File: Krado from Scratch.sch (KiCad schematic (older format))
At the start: 12 parts

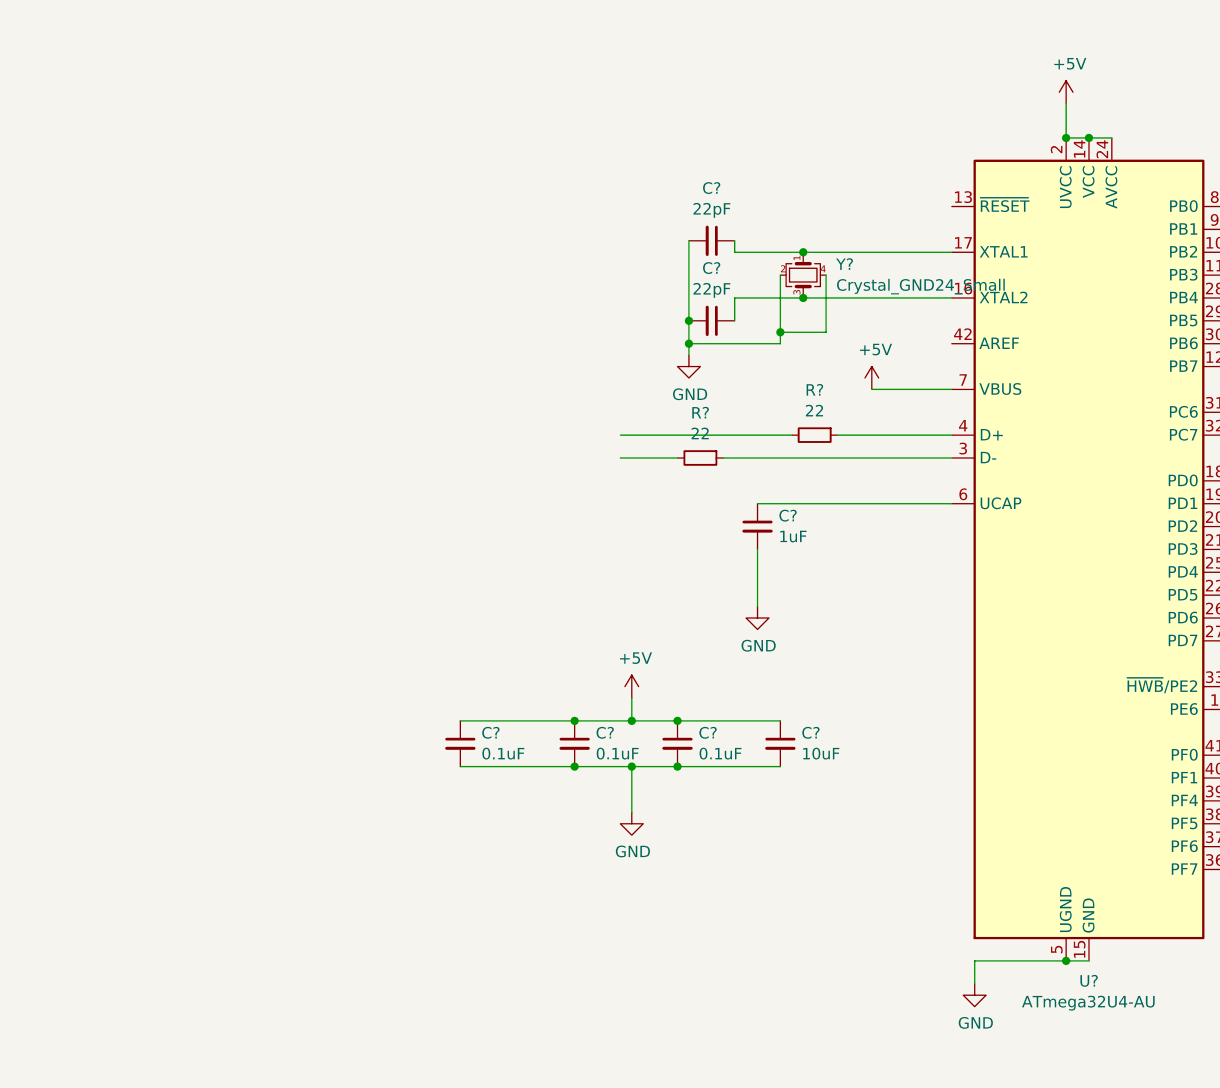
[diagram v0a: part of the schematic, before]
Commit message: USB-C Added
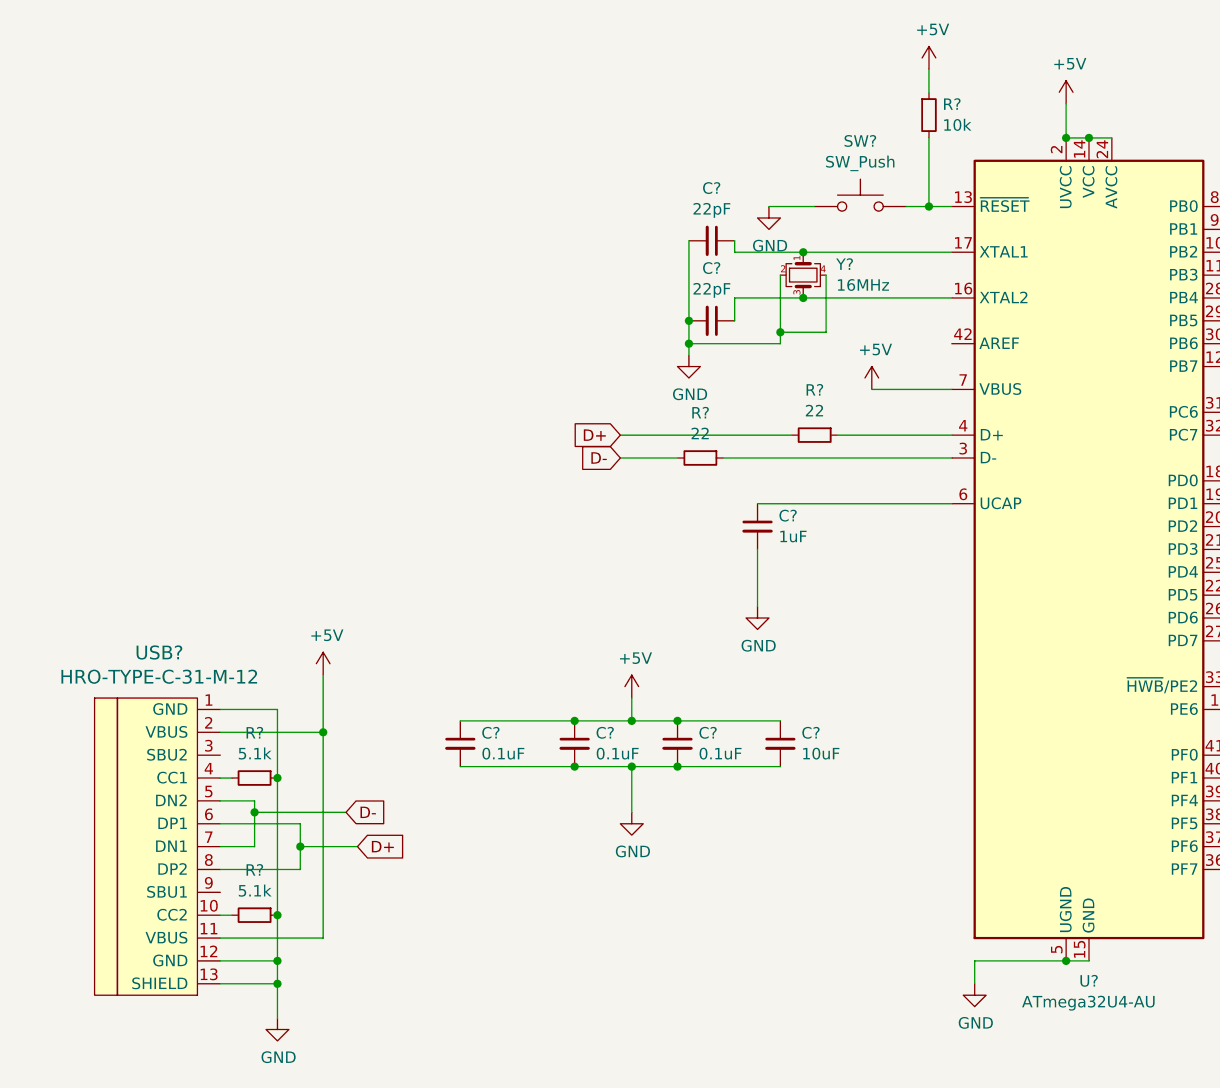
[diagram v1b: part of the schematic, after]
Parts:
- added R?: 10k, symbol Device:R_Small
- added R? (x2): 5.1k, symbol Device:R_Small
- added SW?: SW_Push, symbol Switch:SW_Push
- added USB?: HRO-TYPE-C-31-M-12, symbol Type-C:HRO-TYPE-C-31-M-12
- Y?: value Crystal_GND24_Small -> 16MHz
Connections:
- net labels added: D+, D-
- wire segments 39 -> 68
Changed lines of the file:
@@
 P 9150 3200
 F 0 "Y?" V 9104 3344 50  0000 L CNN
-F 1 "Crystal_GND24_Small" V 9195 3344 50  0000 L CNN
+F 1 "16MHz" V 9195 3344 50  0000 L CNN
 F 2 "" H 9150 3200 50  0001 C CNN
 F 3 "~" H 9150 3200 50  0001 C CNN
@@
 Wire Wire Line
 	9050 3450 9050 3500
+$Comp
+L Switch:SW_Push SW?
+U 1 1 60753B4A
+P 9400 2900
+F 0 "SW?" H 9400 3185 50  0000 C CNN
+F 1 "SW_Push" H 9400 3094 50  0000 C CNN
+F 2 "" H 9400 3100 50  0001 C CNN
+F 3 "~" H 9400 3100 50  0001 C CNN
+	1    9400 2900
+	1    0    0    -1
+$EndComp
+$Comp
+L power:GND #PWR?
+U 1 1 60755F3E
+P 9000 2900
+F 0 "#PWR?" H 9000 2650 50  0001 C CNN
+F 1 "GND" H 9005 2727 50  0000 C CNN
+F 2 "" H 9000 2900 50  0001 C CNN
+F 3 "" H 9000 2900 50  0001 C CNN
+	1    9000 2900
+	1    0    0    -1
+$EndComp
+Wire Wire Line
+	9000 2900 9200 2900
+Wire Wire Line
+	9600 2900 9700 2900
+Wire Wire Line
+	9700 2900 9700 2600
+Connection ~ 9700 2900
+Wire Wire Line
+	9700 2900 9800 2900
+$Comp
+L Device:R_Small R?
+U 1 1 60759043
+P 9700 2500
+F 0 "R?" H 9759 2546 50  0000 L CNN
+F 1 "10k" H 9759 2455 50  0000 L CNN
+F 2 "" H 9700 2500 50  0001 C CNN
+F 3 "~" H 9700 2500 50  0001 C CNN
+	1    9700 2500
+	1    0    0    -1
+$EndComp
+$Comp
+L power:+5V #PWR?
+U 1 1 6075A732
+P 9700 2300
+F 0 "#PWR?" H 9700 2150 50  0001 C CNN
+F 1 "+5V" H 9715 2473 50  0000 C CNN
+F 2 "" H 9700 2300 50  0001 C CNN
+F 3 "" H 9700 2300 50  0001 C CNN
+	1    9700 2300
+	1    0    0    -1
+$EndComp
+Wire Wire Line
+	9700 2400 9700 2300
+Text GLabel 8350 3900 0    50   Input ~ 0
+D+
+Text GLabel 8350 4000 0    50   Input ~ 0
+D-
+$Comp
+L Type-C:HRO-TYPE-C-31-M-12 USB?
+U 1 1 6075E2AA
+P 6500 5650
+F 0 "USB?" H 6333 6447 60  0000 C CNN
+F 1 "HRO-TYPE-C-31-M-12" H 6333 6341 60  0000 C CNN
+F 2 "" H 6500 5650 60  0001 C CNN
+F 3 "" H 6500 5650 60  0001 C CNN
+	1    6500 5650
+	1    0    0    -1
+$EndComp
+$Comp
+L power:+5V #PWR?
+U 1 1 60764690
+P 7050 4950
+F 0 "#PWR?" H 7050 4800 50  0001 C CNN
+F 1 "+5V" H 7065 5123 50  0000 C CNN
+F 2 "" H 7050 4950 50  0001 C CNN
+F 3 "" H 7050 4950 50  0001 C CNN
+	1    7050 4950
+	1    0    0    -1
+$EndComp
+Wire Wire Line
+	6600 5200 7050 5200
+Wire Wire Line
+	7050 5200 7050 4950
+Wire Wire Line
+	6600 6100 7050 6100
+Wire Wire Line
+	7050 6100 7050 5200
+Connection ~ 7050 5200
+$Comp
+L power:GND #PWR?
+U 1 1 60767AC1
+P 6850 6450
+F 0 "#PWR?" H 6850 6200 50  0001 C CNN
+F 1 "GND" H 6855 6277 50  0000 C CNN
+F 2 "" H 6850 6450 50  0001 C CNN
+F 3 "" H 6850 6450 50  0001 C CNN
+	1    6850 6450
+	1    0    0    -1
+$EndComp
+Wire Wire Line
+	6600 5100 6850 5100
+Wire Wire Line
+	6600 6200 6850 6200
+Connection ~ 6850 6200
+Wire Wire Line
+	6850 6200 6850 6300
+Wire Wire Line
+	6600 6300 6850 6300
+Connection ~ 6850 6300
+Wire Wire Line
+	6850 6300 6850 6450
+Wire Wire Line
+	6600 5500 6750 5500
+Wire Wire Line
+	6750 5500 6750 5550
+Wire Wire Line
+	6750 5700 6600 5700
+Wire Wire Line
+	6600 5600 6950 5600
+Wire Wire Line
+	6950 5600 6950 5700
+Wire Wire Line
+	6950 5800 6600 5800
+Wire Wire Line
+	6750 5550 7150 5550
+Connection ~ 6750 5550
+Wire Wire Line
+	6750 5550 6750 5700
+Wire Wire Line
+	6950 5700 7200 5700
+Connection ~ 6950 5700
+Wire Wire Line
+	6950 5700 6950 5800
+Text GLabel 7200 5700 2    50   Input ~ 0
+D+
+Text GLabel 7150 5550 2    50   Input ~ 0
+D-
+Wire Wire Line
+	6850 5100 6850 5400
+$Comp
+L Device:R_Small R?
+U 1 1 60777EB7
+P 6750 5400
+F 0 "R?" V 6554 5400 50  0000 C CNN
+F 1 "5.1k" V 6645 5400 50  0000 C CNN
+F 2 "" H 6750 5400 50  0001 C CNN
+F 3 "~" H 6750 5400 50  0001 C CNN
+	1    6750 5400
+	0    1    1    0
+$EndComp
+Connection ~ 6850 5400
+Wire Wire Line
+	6850 5400 6850 6000
+$Comp
+L Device:R_Small R?
+U 1 1 607796CE
+P 6750 6000
+F 0 "R?" V 6554 6000 50  0000 C CNN
+F 1 "5.1k" V 6645 6000 50  0000 C CNN
+F 2 "" H 6750 6000 50  0001 C CNN
+F 3 "~" H 6750 6000 50  0001 C CNN
+	1    6750 6000
+	0    1    1    0
+$EndComp
+Connection ~ 6850 6000
+Wire Wire Line
+	6850 6000 6850 6200
+Wire Wire Line
+	6650 6000 6600 6000
+Wire Wire Line
+	6650 5400 6600 5400
 $EndSCHEMATC

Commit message: MATRI
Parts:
- added D? (x64): SOD-123, symbol Device:D_Small
- added MX? (x69): MX-NoLED, symbol MX_Alps_Hybrid:MX-NoLED
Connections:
- new net: D?.2 (A), MX?.2 (ROW) (x59)
- new net: D?.2 (A), MX?.2 (ROW), MX?.2 (ROW) (x5)
- new net COL0: MX?.1 (COL), MX?.1 (COL)
- new net COL1: MX?.1 (COL), MX?.1 (COL), MX?.1 (COL), MX?.1 (COL), MX?.1 (COL)
- new net COL10: MX?.1 (COL), MX?.1 (COL), MX?.1 (COL), MX?.1 (COL), MX?.1 (COL)
- new net COL11: MX?.1 (COL), MX?.1 (COL), MX?.1 (COL), MX?.1 (COL), MX?.1 (COL)
- new net COL12: MX?.1 (COL), MX?.1 (COL), MX?.1 (COL), MX?.1 (COL), MX?.1 (COL)
- new net COL13: MX?.1 (COL), MX?.1 (COL), MX?.1 (COL), MX?.1 (COL), MX?.1 (COL)
- new net COL14: MX?.1 (COL), MX?.1 (COL), MX?.1 (COL), MX?.1 (COL)
- new net COL15: MX?.1 (COL), MX?.1 (COL), MX?.1 (COL)
- new net COL2: MX?.1 (COL), MX?.1 (COL), MX?.1 (COL), MX?.1 (COL), MX?.1 (COL)
- new net COL3: MX?.1 (COL), MX?.1 (COL), MX?.1 (COL), MX?.1 (COL)
- new net COL4: MX?.1 (COL), MX?.1 (COL), MX?.1 (COL), MX?.1 (COL)
- new net COL5: MX?.1 (COL), MX?.1 (COL), MX?.1 (COL), MX?.1 (COL)
- new net COL6: MX?.1 (COL), MX?.1 (COL), MX?.1 (COL), MX?.1 (COL), MX?.1 (COL)
- new net COL7: MX?.1 (COL), MX?.1 (COL), MX?.1 (COL), MX?.1 (COL)
- new net COL9: MX?.1 (COL), MX?.1 (COL), MX?.1 (COL), MX?.1 (COL)
- new net ROW0: D?.1 (K), D?.1 (K), D?.1 (K), D?.1 (K), D?.1 (K), D?.1 (K), D?.1 (K), D?.1 (K), D?.1 (K), D?.1 (K), D?.1 (K), D?.1 (K), D?.1 (K), D?.1 (K), D?.1 (K)
- new net ROW1: D?.1 (K), D?.1 (K), D?.1 (K), D?.1 (K), D?.1 (K), D?.1 (K), D?.1 (K), D?.1 (K), D?.1 (K), D?.1 (K), D?.1 (K), D?.1 (K), D?.1 (K)
- new net ROW2: D?.1 (K), D?.1 (K), D?.1 (K), D?.1 (K), D?.1 (K), D?.1 (K), D?.1 (K), D?.1 (K), D?.1 (K), D?.1 (K), D?.1 (K), D?.1 (K)
- new net ROW3: D?.1 (K), D?.1 (K), D?.1 (K), D?.1 (K), D?.1 (K), D?.1 (K), D?.1 (K), D?.1 (K), D?.1 (K), D?.1 (K), D?.1 (K), D?.1 (K), D?.1 (K), D?.1 (K)
- new net ROW4: D?.1 (K), D?.1 (K), D?.1 (K), D?.1 (K), D?.1 (K), D?.1 (K), D?.1 (K), D?.1 (K), D?.1 (K), D?.1 (K)
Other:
- moved on the sheet: C?, R?, SW?, U?, USB?, Y?

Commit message: Matrix Fixed
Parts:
- removed D?: SOD-123, symbol Device:D_Small
- removed MX?: MX-NoLED, symbol MX_Alps_Hybrid:MX-NoLED
- added D? (x4): SOD-123, symbol Device:D_Small
- added KY_8, KY_I, MX? (x2): MX-NoLED, symbol MX_Alps_Hybrid:MX-NoLED
- gave numbers to parts that had none: 28
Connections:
- net COL1: now also MX?.1 (COL)
- net COL10: now also MX?.1 (COL)
- net COL11: now also MX?.1 (COL)
- net COL12: now also MX?.1 (COL)
- net COL14: now also MX?.1 (COL)
- net COL9: now also KY_8.1 (COL); no longer KY_7.1 (COL), KY_U.1 (COL), MX?.1 (COL), MX?.1 (COL)
- net ROW0: now also D?.1 (K)
- net ROW1: now also D?.1 (K)
- net ROW2: now also D?.1 (K)
- net ROW3: now also D?.1 (K)
- new net: D?.2 (A), KY_8.2 (ROW)
- new net: D?.2 (A), KY_I.2 (ROW)
- new net: D?.2 (A), MX?.2 (ROW) (x2)
- new net COL8: KY_7.1 (COL), KY_U.1 (COL), MX?.1 (COL), MX?.1 (COL)
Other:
- moved on the sheet: BACKSPLIT1, BACKSPLIT2, D?, KY_0, KY_9, KY_BAR, KY_EQUALS, KY_LBRACK, KY_MINUS, KY_O, KY_P, KY_RBRACK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

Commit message: Matrix Named
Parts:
- gave numbers to parts that had none: 40
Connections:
- net COL9: now also KY_COMMA.1 (COL), KY_I.1 (COL), KY_K.1 (COL)

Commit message: PCB Generated
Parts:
- added F1: 500mA, Fuse:Fuse_1206_3216Metric, symbol Device:Polyfuse_Small
- 1.25U_PN2, 1.25U_R_ALT1: renamed from MX?; footprint (none) -> MX_Only:MXOnly-1.25U-Hotswap
- 1U_PN1: renamed from PN; footprint (none) -> MX_Only:MXOnly-1U-Hotswap
- 1U_R_ALT1: renamed from R_ALT; footprint (none) -> MX_Only:MXOnly-1U-Hotswap
- 2.75U_SHIFT1: renamed from 2.75U_SHIFT; footprint (none) -> MX_Only:MXOnly-2.75U-Hotswap
- 2U_BACKSPACE1: renamed from 2U_BACKSPACE; footprint (none) -> MX_Only:MXOnly-2U-Hotswap
- BACKSPLIT1, BACKSPLIT2, KY_0, KY_1, KY_2, KY_3, KY_4, KY_5, KY_6, KY_7, KY_8, KY_9: footprint (none) -> MX_Only:MXOnly-1U-Hotswap
- C1, C2, C3, C4, C5, C6, C7: renamed from C?; footprint (none) -> Diode_SMD:D_SOD-123
- D1, D10, D11, D12, D13, D14, D15, D16, D17, D18, D19, D2, D20, D21, D22, D23, D24, D25, D26, D27, D28, D29, D3, D30, D31, D32, D33, D34, D35, D36, D37, D38, D39, D4, D40, D41, D42, D43, D44, D45, D46, D47, D48, D49, D5, D50, D51, D52, D53, D54, D55, D56, D57, D58, D59, D6, D60, D61, D62, D63, D64, D65, D66, D67, D7, D8, D9: renamed from D?; footprint (none) -> Diode_SMD:D_SOD-123
- DOWNARROW1: renamed from DOWNARROW; footprint (none) -> MX_Only:MXOnly-1U-Hotswap
- FN1: renamed from FN; footprint (none) -> MX_Only:MXOnly-1U-Hotswap
- KY_A1: renamed from KY_A; footprint (none) -> MX_Only:MXOnly-1U-Hotswap
- KY_B1: renamed from KY_B; footprint (none) -> MX_Only:MXOnly-1U-Hotswap
- KY_BAR1: renamed from KY_BAR; footprint (none) -> MX_Only:MXOnly-1U-Hotswap
- KY_C1: renamed from KY_C; footprint (none) -> MX_Only:MXOnly-1U-Hotswap
- KY_COLON1: renamed from KY_COLON; footprint (none) -> MX_Only:MXOnly-1U-Hotswap
- KY_COMMA1: renamed from KY_COMMA; footprint (none) -> MX_Only:MXOnly-1U-Hotswap
- KY_D1: renamed from KY_D; footprint (none) -> MX_Only:MXOnly-1U-Hotswap
- KY_E1: renamed from KY_E; footprint (none) -> MX_Only:MXOnly-1U-Hotswap
- KY_EQUALS1: renamed from KY_EQUALS; footprint (none) -> MX_Only:MXOnly-1U-Hotswap
- KY_ESC1: renamed from KY_ESC; footprint (none) -> MX_Only:MXOnly-1U-Hotswap
- KY_F1: renamed from KY_F; footprint (none) -> MX_Only:MXOnly-1U-Hotswap
- KY_G1: renamed from KY_G; footprint (none) -> MX_Only:MXOnly-1U-Hotswap
- KY_GRAVE1: renamed from KY_GRAVE; footprint (none) -> MX_Only:MXOnly-1U-Hotswap
- KY_H1: renamed from KY_H; footprint (none) -> MX_Only:MXOnly-1U-Hotswap
- KY_I1: renamed from KY_I; footprint (none) -> MX_Only:MXOnly-1U-Hotswap
- KY_J1: renamed from KY_J; footprint (none) -> MX_Only:MXOnly-1U-Hotswap
- KY_K1: renamed from KY_K; footprint (none) -> MX_Only:MXOnly-1U-Hotswap
- KY_L1: renamed from KY_L; footprint (none) -> MX_Only:MXOnly-1U-Hotswap
- KY_LBRACK1: renamed from KY_LBRACK; footprint (none) -> MX_Only:MXOnly-1U-Hotswap
- KY_M1: renamed from KY_M; footprint (none) -> MX_Only:MXOnly-1U-Hotswap
- KY_MINUS1: renamed from KY_MINUS; footprint (none) -> MX_Only:MXOnly-1U-Hotswap
- KY_N1: renamed from KY_N; footprint (none) -> MX_Only:MXOnly-1U-Hotswap
- KY_O1: renamed from KY_O; footprint (none) -> MX_Only:MXOnly-1U-Hotswap
- KY_P1: renamed from KY_P; footprint (none) -> MX_Only:MXOnly-1U-Hotswap
- KY_PERIOD1: renamed from KY_PERIOD; footprint (none) -> MX_Only:MXOnly-1U-Hotswap
- KY_Q1: renamed from KY_Q; footprint (none) -> MX_Only:MXOnly-1U-Hotswap
- KY_QUESTION1: renamed from KY_QUESTION; footprint (none) -> MX_Only:MXOnly-1U-Hotswap
- KY_QUOTE1: renamed from KY_QUOTE; footprint (none) -> MX_Only:MXOnly-1U-Hotswap
- KY_R1: renamed from KY_R; footprint (none) -> MX_Only:MXOnly-1U-Hotswap
- KY_RBRACK1: renamed from KY_RBRACK; footprint (none) -> MX_Only:MXOnly-1U-Hotswap
- KY_S1: renamed from KY_S; footprint (none) -> MX_Only:MXOnly-1U-Hotswap
- KY_T1: renamed from KY_T; footprint (none) -> MX_Only:MXOnly-1U-Hotswap
- KY_U1: renamed from KY_U; footprint (none) -> MX_Only:MXOnly-1U-Hotswap
- KY_V1: renamed from KY_V; footprint (none) -> MX_Only:MXOnly-1U-Hotswap
- KY_W1: renamed from KY_W; footprint (none) -> MX_Only:MXOnly-1U-Hotswap
- KY_X1: renamed from KY_X; footprint (none) -> MX_Only:MXOnly-1U-Hotswap
- KY_Y1: renamed from KY_Y; footprint (none) -> MX_Only:MXOnly-1U-Hotswap
- KY_Z1: renamed from KY_Z; footprint (none) -> MX_Only:MXOnly-1U-Hotswap
- LEFTARROW1: renamed from LEFTARROW; footprint (none) -> MX_Only:MXOnly-1U-Hotswap
- L_ALT1: renamed from L_ALT; footprint (none) -> MX_Only:MXOnly-1.25U-Hotswap
- L_CTRL1: renamed from L_CTRL; footprint (none) -> MX_Only:MXOnly-1.25U-Hotswap
- L_GUI1: renamed from L_GUI; footprint (none) -> MX_Only:MXOnly-1.25U-Hotswap
- MOD_ENTER1: renamed from KY_ENTER; footprint (none) -> MX_Only:MXOnly-2.25U-Hotswap
- MOD_L_SHIFT1: renamed from L_SHIFT; footprint (none) -> MX_Only:MXOnly-2.25U-Hotswap
- MOD_R_SHIFT1: renamed from R_SHIFT; footprint (none) -> MX_Only:MXOnly-1.75U-Hotswap
- MOD_TAB1: renamed from KY_TAB; footprint (none) -> MX_Only:MXOnly-1.5U-Hotswap
- MOD_TAB2: renamed from KY_CAPS; footprint (none) -> MX_Only:MXOnly-1.75U-Hotswap
- R1, R2, R3, R4, R5, R6: renamed from R?; footprint (none) -> Resistor_SMD:R_0805_2012Metric
- RIGHTARROW1: renamed from RIGHTARROW; footprint (none) -> MX_Only:MXOnly-1U-Hotswap
- R_CTRL1: renamed from R_CTRL; footprint (none) -> MX_Only:MXOnly-1U-Hotswap
- SPACE1: renamed from SPACE; footprint (none) -> MX_Only:MXOnly-6.25U-Hotswap
- STEPPED_CAPS1: renamed from STEPPED_CAPS; footprint (none) -> MX_Only:MXOnly-1U-Hotswap
- SW1: renamed from SW?; footprint (none) -> random-keyboard-parts:SKQG-1155865
- UPARROW1: renamed from UPARROW; footprint (none) -> MX_Only:MXOnly-1U-Hotswap
- USB1: renamed from USB?; footprint (none) -> Type-C:HRO-TYPE-C-31-M-12
- Y1: renamed from Y?; footprint (none) -> Crystal:Crystal_SMD_3225-4Pin_3.2x2.5mm
- gave numbers to parts that had none: 1
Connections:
- net +5V: now also F1.1; no longer USB1.11 (VBUS), USB1.2 (VBUS)
- new net VCC: F1.2, USB1.11 (VBUS), USB1.2 (VBUS)
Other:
- moved on the sheet: 1.25U_PN2, 1.25U_R_ALT1, 1U_PN1, 1U_R_ALT1, 2.75U_SHIFT1, 2U_BACKSPACE1, BACKSPLIT1, BACKSPLIT2, C1, C2, C3, C4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

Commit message: PCB Switches Layout
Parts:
- renumbered MOD_TAB2 to MOD_CAPS1
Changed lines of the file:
@@
 $EndComp
 $Comp
-L MX_Alps_Hybrid:MX-NoLED MOD_TAB2
+L MX_Alps_Hybrid:MX-NoLED MOD_CAPS1
 U 1 1 60881753
 P 5350 6250
-F 0 "MOD_TAB2" H 5383 6473 60  0000 C CNN
+F 0 "MOD_CAPS1" H 5383 6473 60  0000 C CNN
 F 1 "MX-NoLED" H 5383 6399 20  0000 C CNN
 F 2 "MX_Only:MXOnly-1.75U-Hotswap" H 4725 6225 60  0001 C CNN

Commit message: PCB Mapped
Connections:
- net COL0: now also U1.29 (PB5)
- net COL1: now also U1.30 (PB6)
- net COL10: now also U1.22 (PD5)
- net COL11: now also U1.26 (PD6)
- net COL12: now also U1.27 (PD7)
- net COL13: now also U1.41 (PF0)
- net COL14: now also U1.40 (PF1)
- net COL15: now also U1.39 (PF4)
- net COL2: now also U1.12 (PB7)
- net COL3: now also U1.31 (PC6)
- net COL4: now also U1.32 (PC7)
- net COL5: now also U1.18 (PD0)
- net COL6: now also U1.19 (PD1)
- net COL7: now also U1.20 (PD2)
- net COL8: now also U1.21 (PD3)
- net COL9: now also U1.25 (PD4)
- net ROW0: now also U1.8 (PB0)
- net ROW1: now also U1.9 (PB1)
- net ROW2: now also U1.10 (PB2)
- net ROW3: now also U1.11 (PB3)
- net ROW4: now also U1.28 (PB4)
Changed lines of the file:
@@
 Wire Wire Line
 	17750 7650 17750 7550
+Text GLabel 21050 7450 2    50   Input ~ 0
+ROW0
+Text GLabel 21050 7550 2    50   Input ~ 0
+ROW1
+Text GLabel 21050 7650 2    50   Input ~ 0
+ROW2
+Text GLabel 21050 7750 2    50   Input ~ 0
+ROW3
+Text GLabel 21050 7850 2    50   Input ~ 0
+ROW4
+Text GLabel 21050 7950 2    50   Input ~ 0
+COL0
+Text GLabel 21050 8050 2    50   Input ~ 0
+COL1
+Text GLabel 21050 8150 2    50   Input ~ 0
+COL2
+Text GLabel 21050 8350 2    50   Input ~ 0
+COL3
+Text GLabel 21050 8450 2    50   Input ~ 0
+COL4
+Text GLabel 21050 8650 2    50   Input ~ 0
+COL5
+Text GLabel 21050 8750 2    50   Input ~ 0
+COL6
+Text GLabel 21050 8850 2    50   Input ~ 0
+COL7
+Text GLabel 21050 8950 2    50   Input ~ 0
+COL8
+Text GLabel 21050 9050 2    50   Input ~ 0
+COL9
+Text GLabel 21050 9150 2    50   Input ~ 0
+COL10
+Text GLabel 21050 9250 2    50   Input ~ 0
+COL11
+Text GLabel 21050 9350 2    50   Input ~ 0
+COL12
+Text GLabel 21050 9850 2    50   Input ~ 0
+COL13
+Text GLabel 21050 9950 2    50   Input ~ 0
+COL14
+Text GLabel 21050 10050 2    50   Input ~ 0
+COL15
 $EndSCHEMATC
